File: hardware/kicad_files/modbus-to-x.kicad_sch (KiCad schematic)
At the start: 50 parts, among them IC1 ESP32-WROOM-32D_M113DH2800PH3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, J1 2_54mm_PinHeader1x4, J3 Screw_Terminal_3.5mm_4, J4 M50-3140645R, Q1 DSS4160U-7, Q2 DSS4160U-7, SW3 3983, SW4 3983, U3 MAX3485, U4 TPS563208DDCT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

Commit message: final alpha_v0.2
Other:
- moved on the sheet: RX2_TP1, TX2_TP2
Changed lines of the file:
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@@
 	)
 	(label "TX_{2}"
-		(at 213.36 125.73 180)
+		(at 210.185 131.445 180)
 		(effects
 			(font
@@
 	)
 	(label "RX_{2}"
-		(at 213.36 119.38 180)
+		(at 210.185 125.095 180)
 		(effects
 			(font
@@
 	(symbol
 		(lib_id "KEYSTONE_5029:5029")
-		(at 218.44 125.73 0)
+		(at 215.265 131.445 0)
 		(unit 1)
 		(exclude_from_sim no)
@@
 		(fields_autoplaced yes)
 		(property "Reference" "TX2_TP2"
-			(at 220.98 124.4599 0)
+			(at 217.805 130.1749 0)
 			(effects
 				(font
@@
 		)
 		(property "Value" "5029"
-			(at 220.98 126.9999 0)
+			(at 217.805 132.7149 0)
 			(effects
 				(font
@@
 		)
 		(property "Footprint" "project_footprints:KEYSTONE_5029"
-			(at 218.44 125.73 0)
+			(at 215.265 131.445 0)
 			(effects
 				(font
@@
 		)
 		(property "Datasheet" "https://www.keyelco.com/product-pdf.cfm?p=1358"
-			(at 218.44 125.73 0)
+			(at 215.265 131.445 0)
 			(effects
 				(font
@@
 		)
 		(property "Description" "PC Test Point, Miniature Phosphor Bronze Silver Plating Surface Mount Mounting Type"
-			(at 218.44 125.73 0)
+			(at 215.265 131.445 0)
 			(effects
 				(font
@@
 		)
 		(property "PartNo" "5029"
-			(at 218.44 125.73 0)
+			(at 215.265 131.445 0)
 			(effects
 				(font
@@
 	(symbol
 		(lib_id "KEYSTONE_5029:5029")
-		(at 218.44 119.38 0)
+		(at 215.265 125.095 0)
 		(unit 1)
 		(exclude_from_sim no)
@@
 		(fields_autoplaced yes)
 		(property "Reference" "RX2_TP1"
-			(at 220.98 118.1099 0)
+			(at 217.805 123.8249 0)
 			(effects
 				(font
@@
 		)
 		(property "Value" "5029"
-			(at 220.98 120.6499 0)
+			(at 217.805 126.3649 0)
 			(effects
 				(font
@@
 		)
 		(property "Footprint" "project_footprints:KEYSTONE_5029"
-			(at 218.44 119.38 0)
+			(at 215.265 125.095 0)
 			(effects
 				(font
@@
 		)
 		(property "Datasheet" "https://www.keyelco.com/product-pdf.cfm?p=1358"
-			(at 218.44 119.38 0)
+			(at 215.265 125.095 0)
 			(effects
 				(font
@@
 		)
 		(property "Description" "PC Test Point, Miniature Phosphor Bronze Silver Plating Surface Mount Mounting Type"
-			(at 218.44 119.38 0)
+			(at 215.265 125.095 0)
 			(effects
 				(font
@@
 		)
 		(property "PartNo" "5029"
-			(at 218.44 119.38 0)
+			(at 215.265 125.095 0)
 			(effects
 				(font

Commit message: new ps
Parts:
- removed C1, C9: 0.1uF, Capacitor_SMD:C_1206_3216Metric_Pad1.33x1.80mm_HandSolder, symbol Device:C
- removed C23, C26: 10uF, Capacitor_SMD:C_0805_2012Metric_Pad1.18x1.45mm_HandSolder, symbol Device:C
- removed C27, C28, C29: 22uF, Capacitor_SMD:C_0603_1608Metric_Pad1.08x0.95mm_HandSolder, symbol Device:C
- removed J1: 2_54mm_PinHeader1x4, Connector_PinHeader_2.54mm:PinHeader_1x04_P2.54mm_Vertical, symbol SparkFun-Connector:Screw_Terminal_3.5mm_4
- removed J3: Screw_Terminal_3.5mm_4, TerminalBlock_4Ucon:TerminalBlock_4Ucon_1x04_P3.50mm_Horizontal, symbol SparkFun-Connector:Screw_Terminal_3.5mm_4
- removed L2: 2uH, project_footprints:SRN8040-2R2Y, symbol Device:L
- removed R13, R22, R5: 10K, Resistor_SMD:R_0805_2012Metric_Pad1.20x1.40mm_HandSolder, symbol Device:R
- removed R21: 33.2K, Resistor_SMD:R_0805_2012Metric_Pad1.20x1.40mm_HandSolder, symbol Device:R
- removed RX2_TP1, TX2_TP2, VOUT_TP1: 5029, project_footprints:KEYSTONE_5029, symbol KEYSTONE_5029:5029
- removed SW3: 3983, project_footprints:SW_3983_ADA, symbol Adafruit 3983 Mini Soft Touch Switch:3983
- removed U4: TPS563208DDCT, project_footprints:TPS563208DDCT_SOT95P280X110-6N, symbol Buck Converter TPS563208DDCT:TPS563208DDCT
- added C6: 100uF, project_footprints:25SVPF100M, symbol Device:C_Polarized
- added C8: 680uF, project_footprints:EEV-FK1V681Q, symbol Device:C_Polarized
- added D2: B340LA-13-F, Diode_SMD:D_SMA_Handsoldering, symbol Diode:SMAJ12A
- added J1: 615006138421, project_footprints:RJ12_615006138421, symbol RJ12_615006138421:615006138421
- added L1: 33uH, project_footprints:7447709330, symbol Device:L
- added SW1: SW_Wuerth_450301014042, Button_Switch_THT:SW_Slide-03_Wuerth-WS-SLTV_10x2.5x6.4_P2.54mm, symbol Switch:SW_Wuerth_450301014042
- added U1: LM2596S-3.3, Package_TO_SOT_SMD:TO-263-5_TabPin3, symbol Regulator_Switching:LM2596S-3.3
- J4: value M50-3140645R -> M50-3140545R; footprint project_footprints:HARWIN_M50-3140645R -> project_footprints:HARWIN_M50-3140545R; symbol M50-3140645R:M50-3140645R -> M50-3140545R:M50-3140545R; MANUFACTURER (none) -> HARWIN; STANDARD (none) -> Manufacturer Recommendations
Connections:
- net GND: now also C6.2, C8.2, D2.2 (A2), J1.1, U1.3 (GND)
- net RS485+: now also J1.5
- net RS485-: now also J1.3
- net VDD33: now also C8.1, L1.1, U1.4 (FB); no longer J4.6
- net VBUS_12 renamed V_IN
- net V_IN: now also J1.6, SW1.1 (B), SW1.2 (C)
- new net: D2.1 (A1), L1.2, U1.2 (OUT)
- new net OFF: U1.5 (~{ON}/OFF)
- new net V_BUCK: C6.1, SW1.3 (A), U1.1 (VIN)
- no-connect marks 19 -> 21
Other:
- note added: "Reset Button"
- note removed: "Boot/Reset Buttons"
- note removed: "I2C Peripheral"
- note removed: "I2C Pull-Up"
- note removed: "Power/Data"
- moved on the sheet: C2, D1, D3, R15, R3, SW4

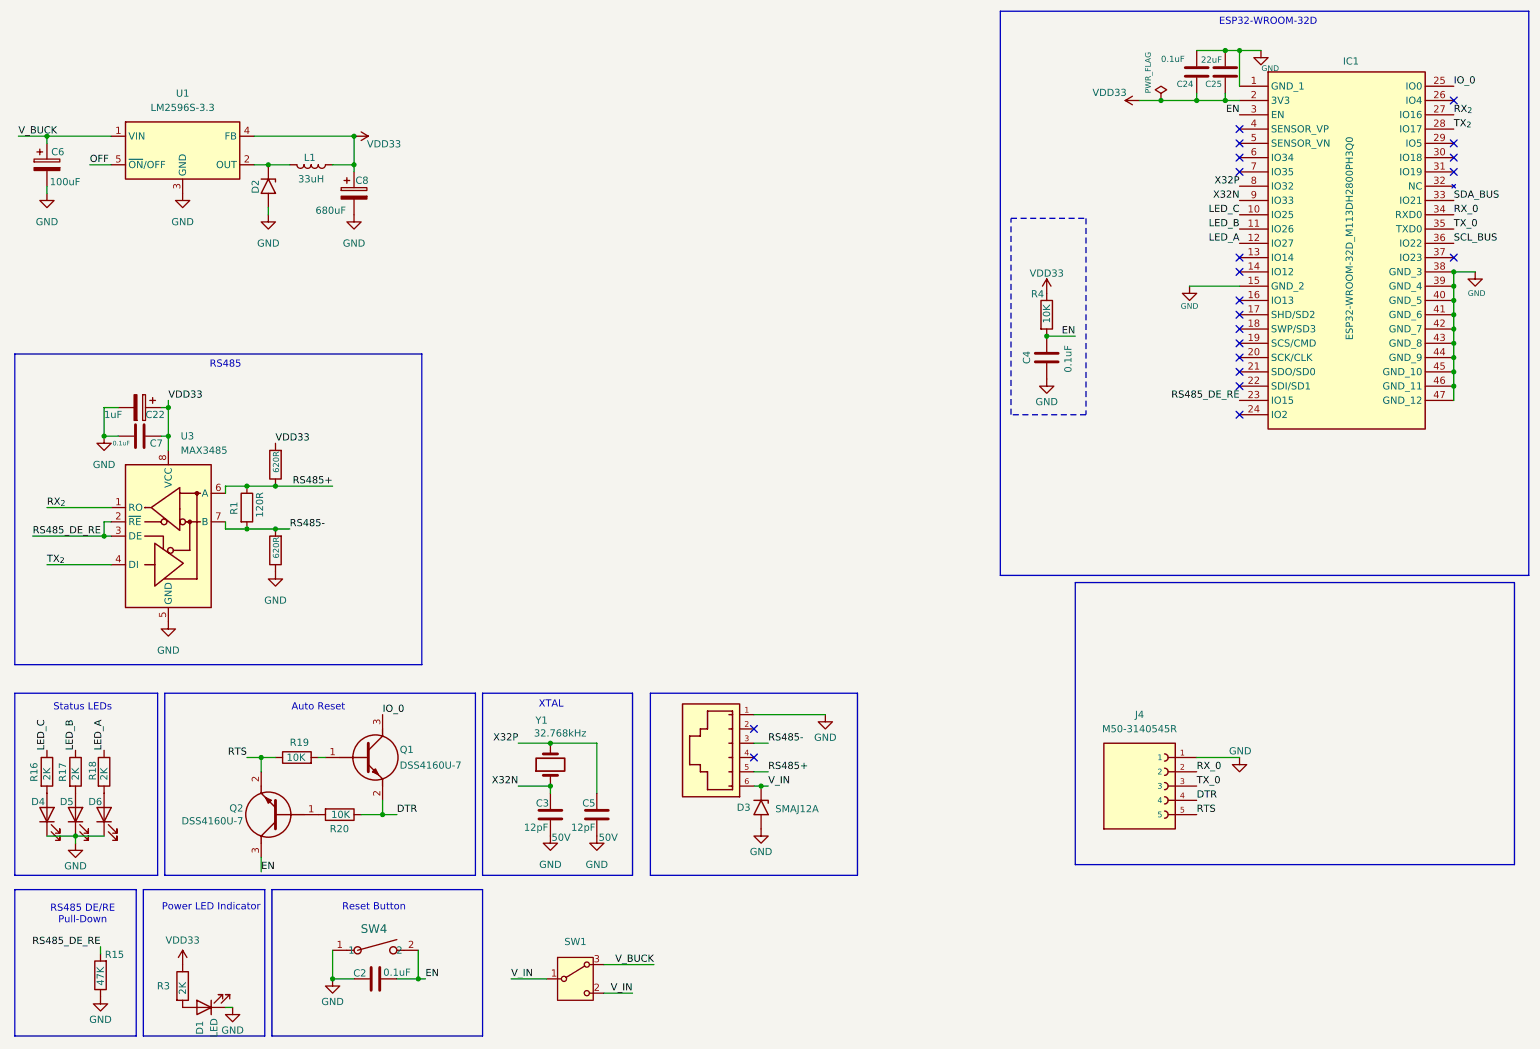
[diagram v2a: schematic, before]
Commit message: improved datapoint alloc. fixed indicator bug
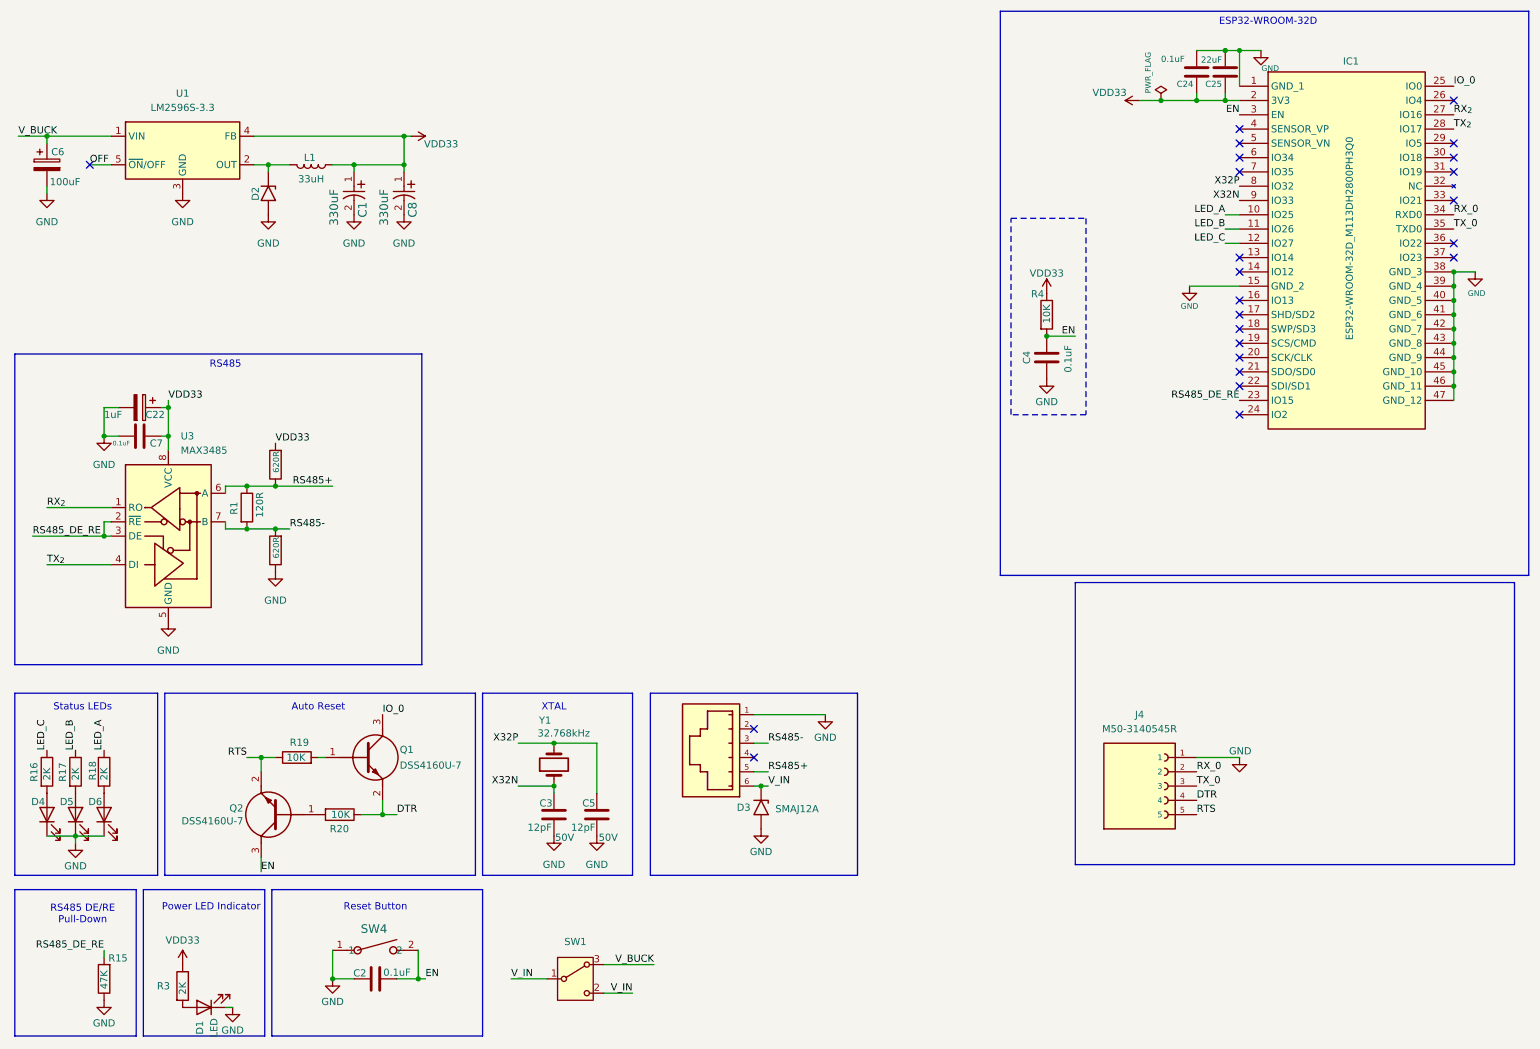
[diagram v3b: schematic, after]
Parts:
- removed C8: 680uF, project_footprints:EEV-FK1V681Q, symbol Device:C_Polarized
- added C1, C8: 330uF, project_footprints:T495D337K006ATE100, symbol Tantalum 330uF T495D337K006ATE100:T495D337K006ATE100
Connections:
- net GND: now also C1.2, C8.2
- net LED_A: now also IC1.10 (IO25); no longer IC1.12 (IO27)
- net LED_C: now also IC1.12 (IO27); no longer IC1.10 (IO25)
- net VDD33: now also C1.1, C8.1
- net SCL_BUS: no longer names the net of IC1.36 (IO22)
- net SDA_BUS: no longer names the net of IC1.33 (IO21)
- no-connect marks 21 -> 24
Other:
- moved on the sheet: C3, D2, R15, Y1
